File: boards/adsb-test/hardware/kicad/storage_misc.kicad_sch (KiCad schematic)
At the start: 0 parts

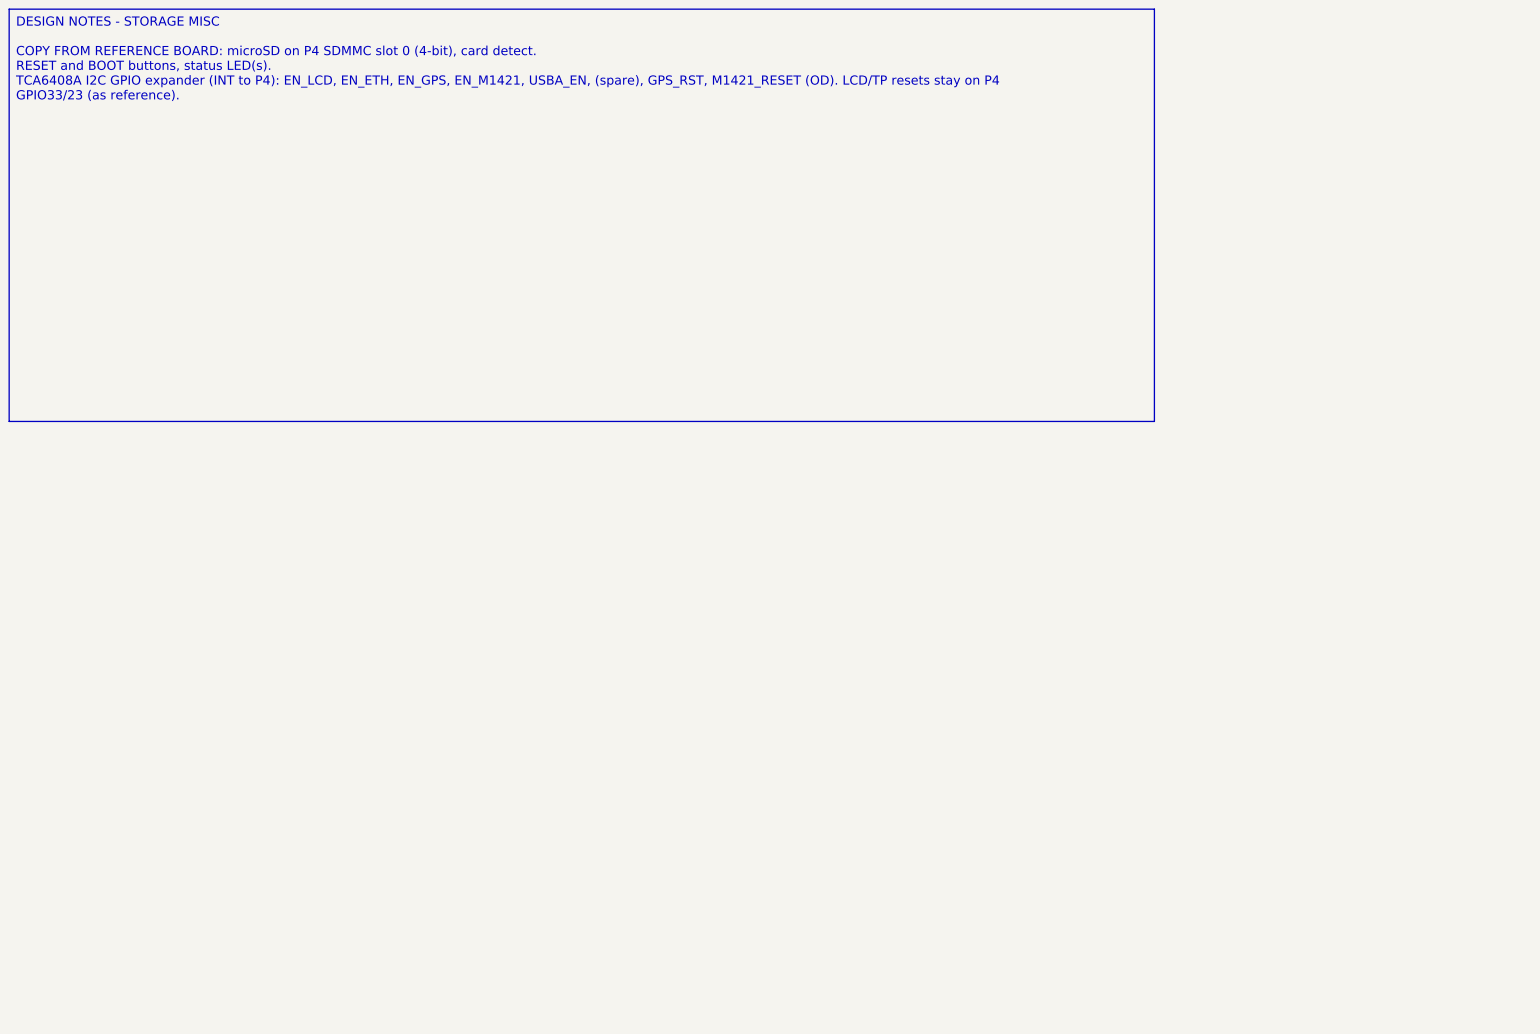
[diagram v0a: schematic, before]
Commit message: Release v0.22.0: all ADSB_Test schematic sheets generated (ERC clean)
Co-Authored-By: Claude Opus 5.5 <noreply@anthropic.com>
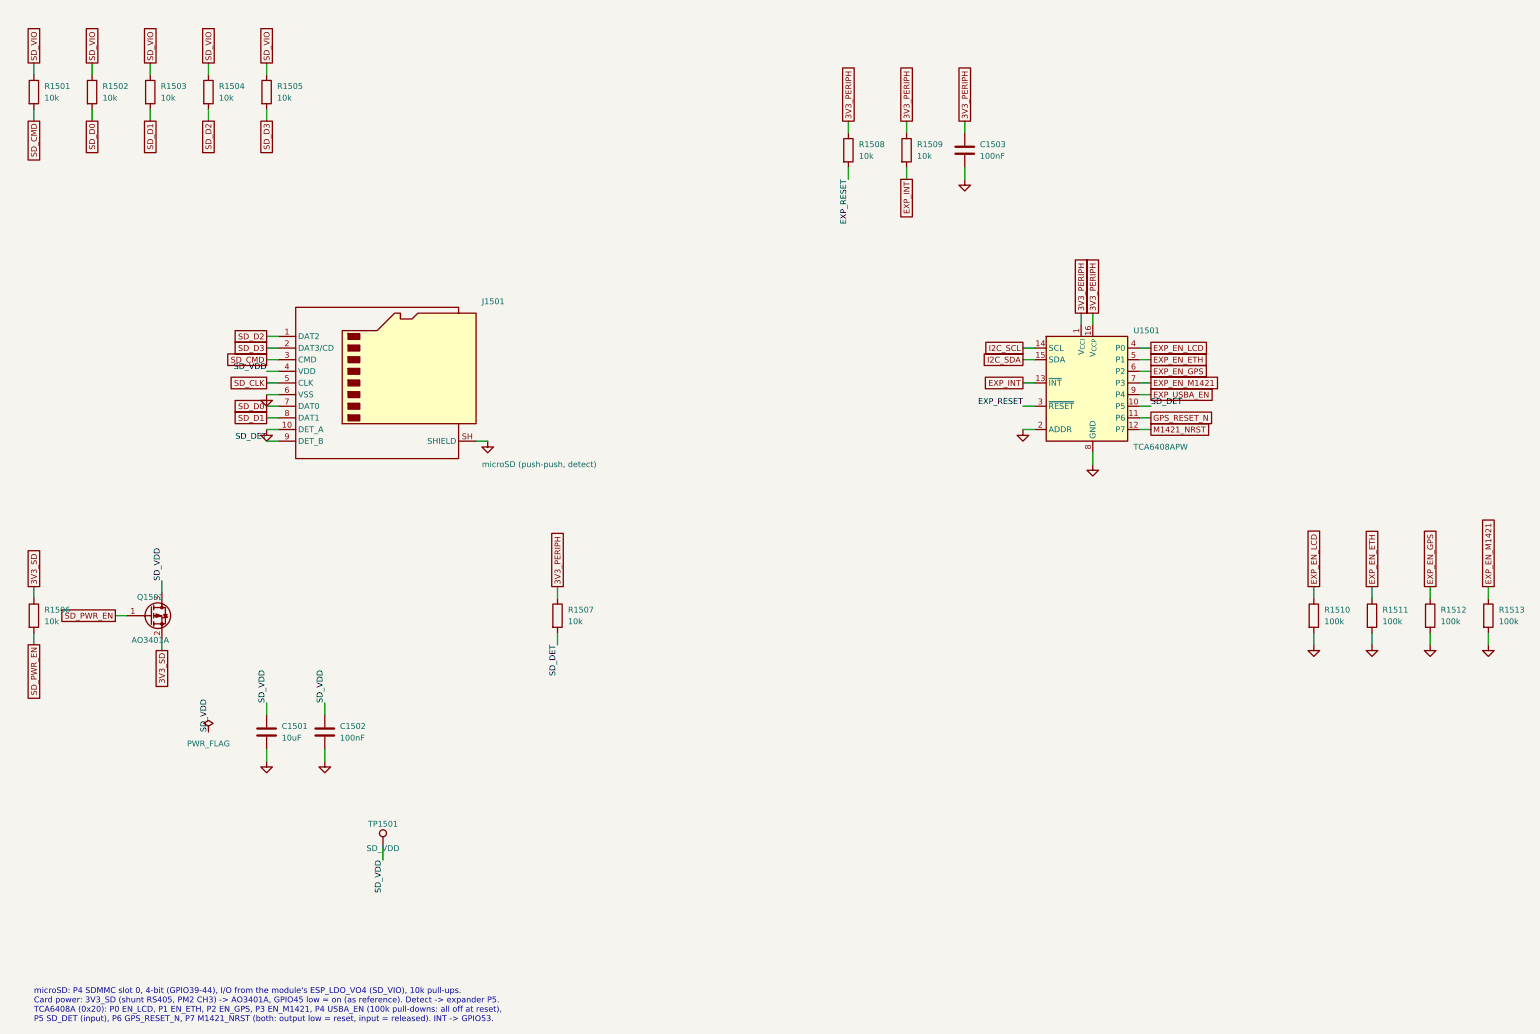
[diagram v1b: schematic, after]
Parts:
- added C1501: 10uF, Capacitor_SMD:C_1206_3216Metric_Pad1.33x1.80mm_HandSolder, symbol Device:C
- added C1502, C1503: 100nF, Capacitor_SMD:C_0805_2012Metric_Pad1.18x1.45mm_HandSolder, symbol Device:C
- added J1501: microSD (push-push, detect), Connector_Card:microSD_HC_Molex_104031-0811, symbol Connector:Micro_SD_Card_Det2
- added Q1501: AO3401A, Package_TO_SOT_SMD:SOT-23_Handsoldering, symbol Transistor_FET:AO3401A
- added R1501, R1502, R1503, R1504, R1505, R1506, R1507, R1508, R1509: 10k, Resistor_SMD:R_0805_2012Metric_Pad1.20x1.40mm_HandSolder, symbol Device:R
- added R1510, R1511, R1512, R1513: 100k, Resistor_SMD:R_0805_2012Metric_Pad1.20x1.40mm_HandSolder, symbol Device:R
- added TP1501: SD_VDD, TestPoint:TestPoint_Pad_D1.5mm, symbol Connector:TestPoint
- added U1501: TCA6408APW, Package_SO:TSSOP-16_4.4x5mm_P0.65mm, symbol Interface_Expansion:TCA6408APW
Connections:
- new net 3V3_PERIPH: C1503.1, R1507.1, R1508.1, R1509.1, U1501.1 (V_{CCI}), U1501.16 (V_{CCP})
- new net 3V3_SD: Q1501.2 (S), R1506.1
- new net EXP_EN_ETH: R1511.1, U1501.5 (P1)
- new net EXP_EN_GPS: R1512.1, U1501.6 (P2)
- new net EXP_EN_LCD: R1510.1, U1501.4 (P0)
- new net EXP_EN_M1421: R1513.1, U1501.7 (P3)
- new net EXP_INT: R1509.2, U1501.13 (~{INT})
- new net EXP_RESET: R1508.2, U1501.3 (~{RESET})
- new net EXP_USBA_EN: U1501.9 (P4)
- new net GND: C1501.2, C1502.2, C1503.2, J1501.10 (DET_A), J1501.6 (VSS), J1501.SH (SHIELD), R1510.2, R1511.2, R1512.2, R1513.2, U1501.2 (ADDR), U1501.8 (GND)
- new net GPS_RESET_N: U1501.11 (P6)
- new net I2C_SCL: U1501.14 (SCL)
- new net I2C_SDA: U1501.15 (SDA)
- new net M1421_NRST: U1501.12 (P7)
- new net SD_CLK: J1501.5 (CLK)
- new net SD_CMD: J1501.3 (CMD), R1501.2
- new net SD_D0: J1501.7 (DAT0), R1502.2
- new net SD_D1: J1501.8 (DAT1), R1503.2
- new net SD_D2: J1501.1 (DAT2), R1504.2
- new net SD_D3: J1501.2 (DAT3/CD), R1505.2
- new net SD_DET: J1501.9 (DET_B), R1507.2, U1501.10 (P5)
- new net SD_PWR_EN: Q1501.1 (G), R1506.2
- new net SD_VDD: C1501.1, C1502.1, J1501.4 (VDD), Q1501.3 (D), TP1501.1
- new net SD_VIO: R1501.1, R1502.1, R1503.1, R1504.1, R1505.1
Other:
- note added: "microSD: P4 SDMMC slot 0, 4-bit (GPIO39-44), I/O from the module's ESP_LDO_VO4 (SD_VIO), 10k pull-ups. Card power: 3V3_SD (shunt RS405, PM2 CH3) -> AO3401A, GPIO45 low = on (as reference). Detect -> expander P5. TCA6408A (0x20): P0 EN_LCD, P1 EN_ETH, P2 EN_GPS, P3 EN_M1421, P4 USBA_EN (100k pull-downs: all off at reset), P5 SD_DET (input), P6 GPS_RESET_N, P7 M1421_NRST (both: output low = reset, 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"

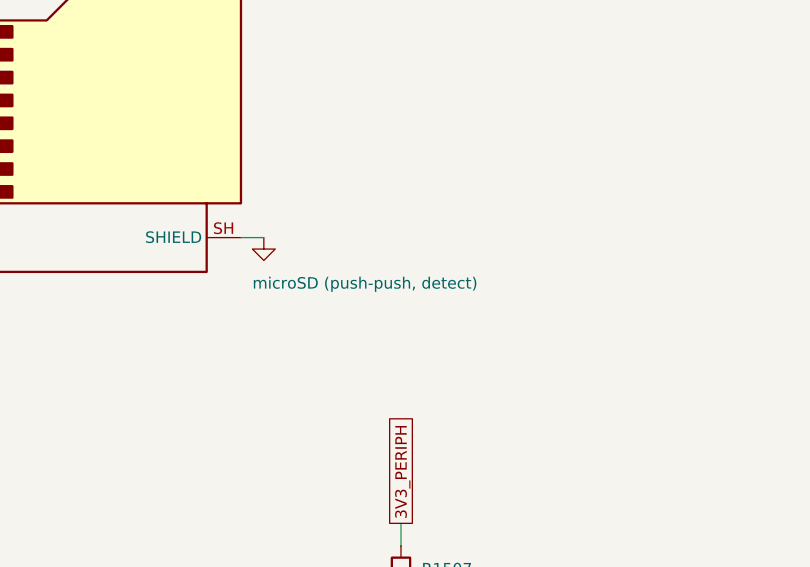
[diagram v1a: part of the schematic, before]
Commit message: Release v0.22.1: LAN8720A strap pull-ups, microSD detect polarity, hand-saved datasheets
Co-Authored-By: Claude Opus 5.5 <noreply@anthropic.com>
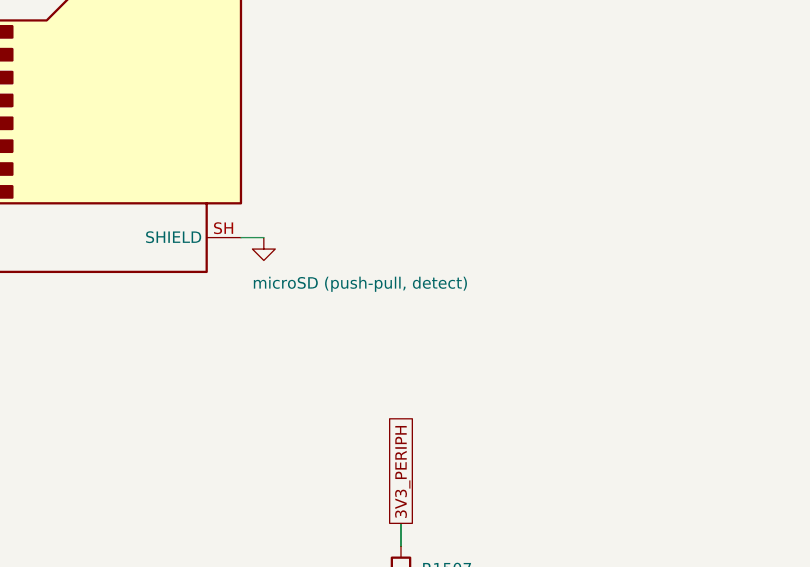
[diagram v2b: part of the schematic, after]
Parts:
- J1501: value microSD (push-push, detect) -> microSD (push-pull, detect); Check Detect switch polarity (closed = card in?) against the Mole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 -> (none); Detect (none) -> Normally-open switch (Molex 104031 spec): closes with a car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
